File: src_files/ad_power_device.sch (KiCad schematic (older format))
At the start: 19 parts, among them J1 SPEAKER, J2 5622-6309-ML, J5 3-1734592-0, J6 3-1734592-0, Q1 DTC143ZEBTL, Q2 DTC143ZEBTL, U7 QUECTEL_L70-RL

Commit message: all screens added_3 items left
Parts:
- removed J5, J6: 3-1734592-0, greencharge-footprints:TE_3-1734592-0, symbol 3-1734592-0:3-1734592-0
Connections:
- no-connect marks 14 -> 13
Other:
- note added: "DISPLAY_ONE \n GPIOs"
- note added: "TO GPS MODULE"
- note added: "TO HDMI"
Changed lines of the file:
@@
 $Descr A3 16535 11693
 encoding utf-8
-Sheet 1 11
+Sheet 1 12
 Title ""
 Date ""
@@
 F39 "LCD_RST_L_GPIO1_C0_DISPLAY_ONE" I L 7175 3500 39
 F40 "TP_RST_L_GPIO1_C2_DISPLAY_ONE" I L 7175 3575 39
-$EndSheet
-$Sheet
-S 1775 4800 1675 525
-U 61B4DD57
-F0 "OTHER_POWER" 50
-F1 "OTHER_POWER.sch" 50
+F41 "HDMITX_CEC_M0" I L 7175 3700 39
+F42 "HDMITX_SDA" I L 7175 3775 39
+F43 "HDMITX_SCL" I L 7175 3850 39
 $EndSheet
 Wire Notes Line
@@
 F25 "LCD_RST_L_GPIO0_C2_DISPLAY_ONE" I R 9075 4850 39
 F26 "TP_RST_L_GPIO0_C5_DISPLAY_ONE" I R 9075 4925 39
+F27 "HDMITX_CEC_M0" I L 7150 5875 39
+F28 "HDMITX_SDA" I L 7150 5950 39
+F29 "HDMITX_SCL" I L 7150 6025 39
 $EndSheet
 Wire Wire Line
@@
 $EndComp
 $Comp
-L 3-1734592-0:3-1734592-0 J5
-U 1 1 63BB8359
-P -2425 10075
-F 0 "J5" V -2050 10025 50  0000 C CNN
-F 1 "3-1734592-0" V -1959 10025 50  0000 C CNN
-F 2 "greencharge-footprints:TE_3-1734592-0" H -2425 10075 50  0001 L BNN
-F 3 "" H -2425 10075 50  0001 L BNN
-F 4 "TE Connectivity" H -2425 10075 50  0001 L BNN "MANUFACTURER"
-F 5 "2.05mm" H -2425 10075 50  0001 L BNN "MAXIMUM_PACKAGE_HEIGHT"
-F 6 "Manufacturer Recommendations" H -2425 10075 50  0001 L BNN "STANDARD"
-F 7 "C" H -2425 10075 50  0001 L BNN "PARTREV"
-	1    -2425 10075
-	0    1    1    0
-$EndComp
-$Comp
-L 3-1734592-0:3-1734592-0 J6
-U 1 1 63BBAD77
-P -2775 11975
-F 0 "J6" V -2400 11925 50  0000 C CNN
-F 1 "3-1734592-0" V -2309 11925 50  0000 C CNN
-F 2 "greencharge-footprints:TE_3-1734592-0" H -2775 11975 50  0001 L BNN
-F 3 "" H -2775 11975 50  0001 L BNN
-F 4 "TE Connectivity" H -2775 11975 50  0001 L BNN "MANUFACTURER"
-F 5 "2.05mm" H -2775 11975 50  0001 L BNN "MAXIMUM_PACKAGE_HEIGHT"
-F 6 "Manufacturer Recommendations" H -2775 11975 50  0001 L BNN "STANDARD"
-F 7 "C" H -2775 11975 50  0001 L BNN "PARTREV"
-	1    -2775 11975
-	0    1    1    0
-$EndComp
-$Comp
 L Mechanical:MountingHole H1
 U 1 1 63BD71C6
@@
 	11700 6250 11700 9850
 NoConn ~ 12275 7825
-NoConn ~ -1650 10275
 Text Label 7025 7625 2    39   ~ 0
 I2C2_SDA_M0_TP
@@
 Wire Wire Line
 	9075 4925 9225 4925
+Text Label 7025 3700 2    39   ~ 0
+HDMITX_CEC_M0
+Text Label 7025 3775 2    39   ~ 0
+HDMITX_SDA
+Text Label 7025 3850 2    39   ~ 0
+HDMITX_SCL
+Wire Wire Line
+	7175 3700 7025 3700
+Wire Wire Line
+	7175 3775 7025 3775
+Wire Wire Line
+	7175 3850 7025 3850
+Text Label 6750 5875 2    39   ~ 0
+HDMITX_CEC_M0
+Text Label 6750 5950 2    39   ~ 0
+HDMITX_SDA
+Text Label 6750 6025 2    39   ~ 0
+HDMITX_SCL
+Wire Wire Line
+	7150 5875 6750 5875
+Wire Wire Line
+	6750 5950 7150 5950
+Wire Wire Line
+	6750 6025 7150 6025
+Wire Notes Line
+	6650 5775 6250 5775
+Wire Notes Line
+	6250 5775 6250 6075
+Wire Notes Line
+	6250 6075 6750 6075
+Text Notes 6250 5800 3    39   ~ 0
+TO HDMI
+$Sheet
+S 1775 4800 1675 525
+U 61B4DD57
+F0 "OTHER_POWER" 50
+F1 "OTHER_POWER.sch" 50
+$EndSheet
+Text Notes 10050 4400 2    39   ~ 0
+TO GPS MODULE
+Wire Notes Line
+	9550 4475 9375 4475
+Wire Notes Line
+	9550 4300 9550 4475
+Wire Notes Line
+	9400 4300 9550 4300
+Wire Notes Line
+	9900 4475 10275 4475
+Wire Notes Line
+	10275 4475 10275 4950
+Wire Notes Line
+	10275 4950 10050 4950
+Text Notes 10400 4925 1    39   ~ 0
+DISPLAY_ONE \n   GPIOs
 $EndSCHEMATC

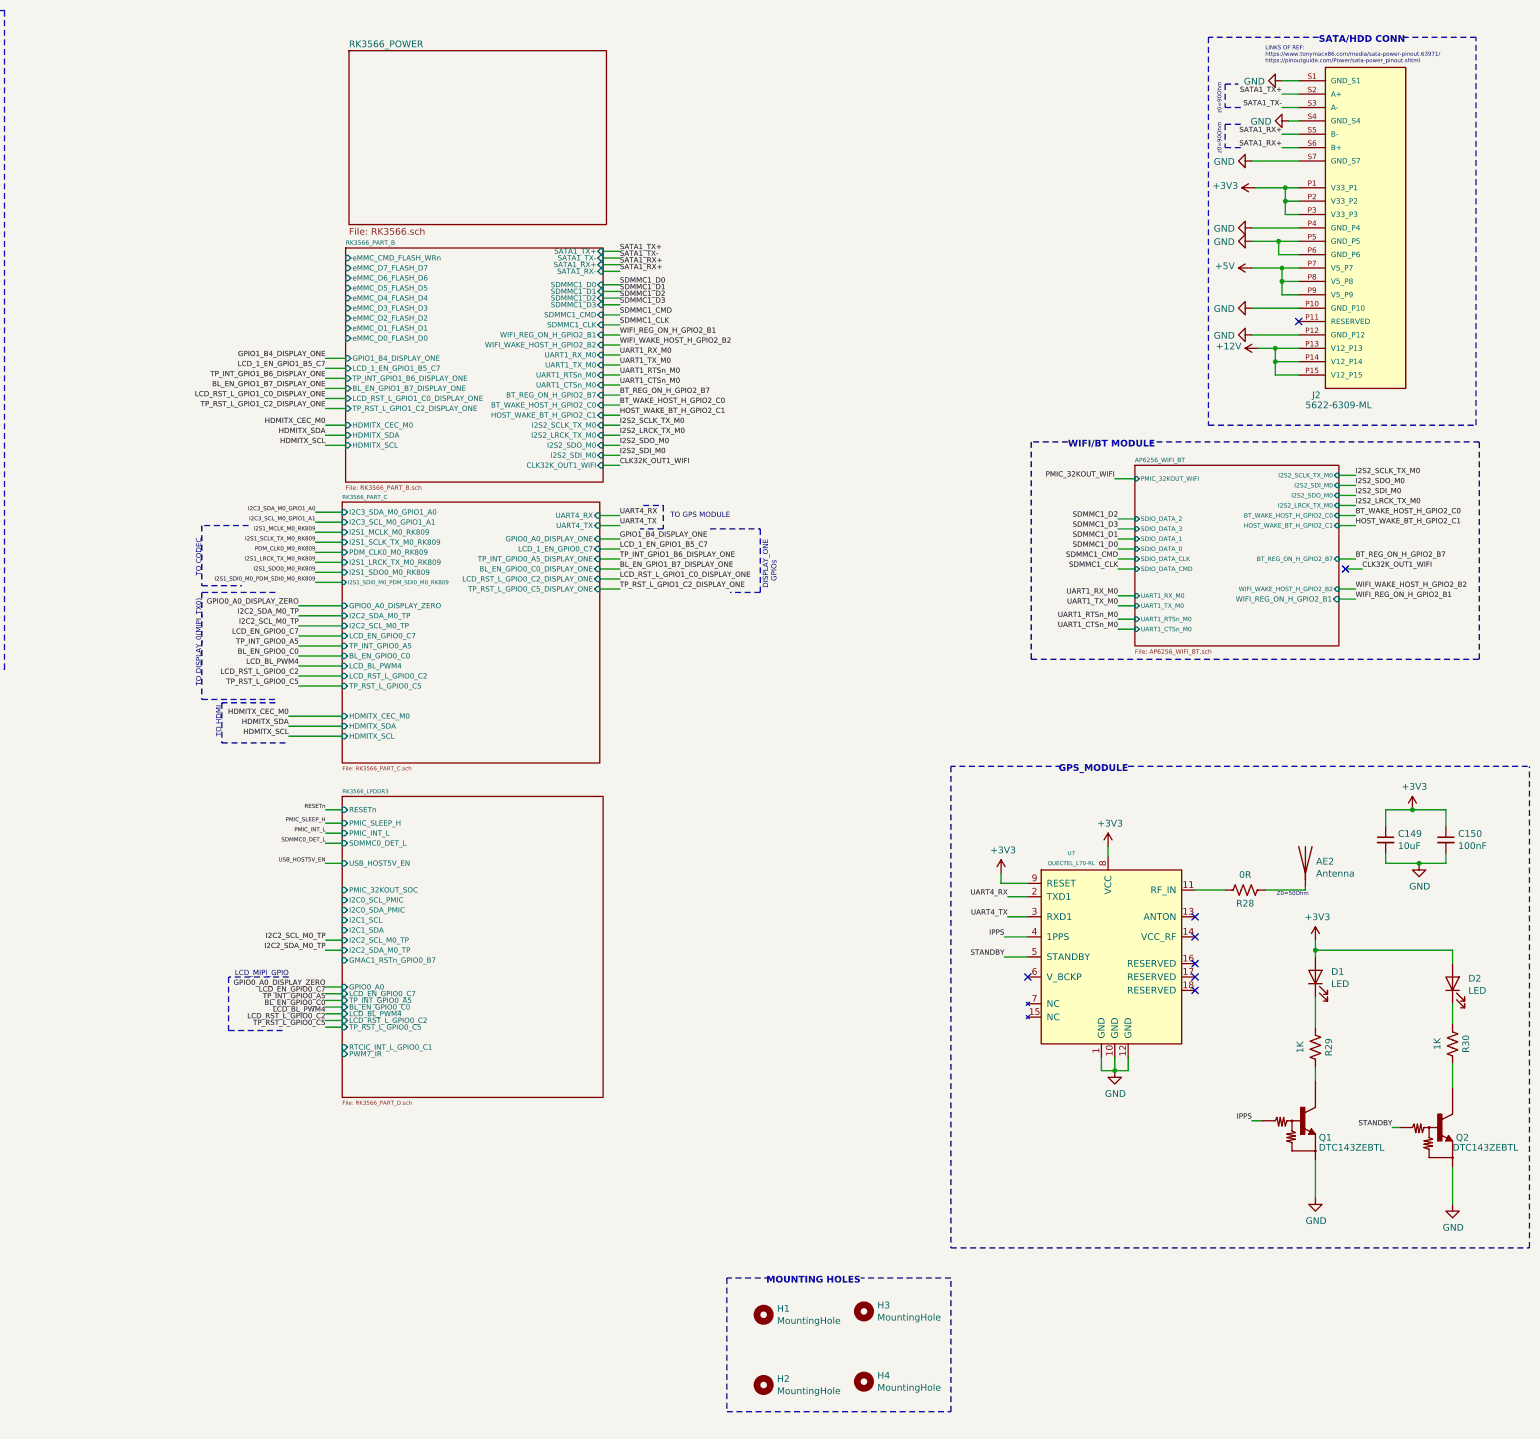
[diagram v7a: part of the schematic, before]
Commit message: updated 4G module and simcard
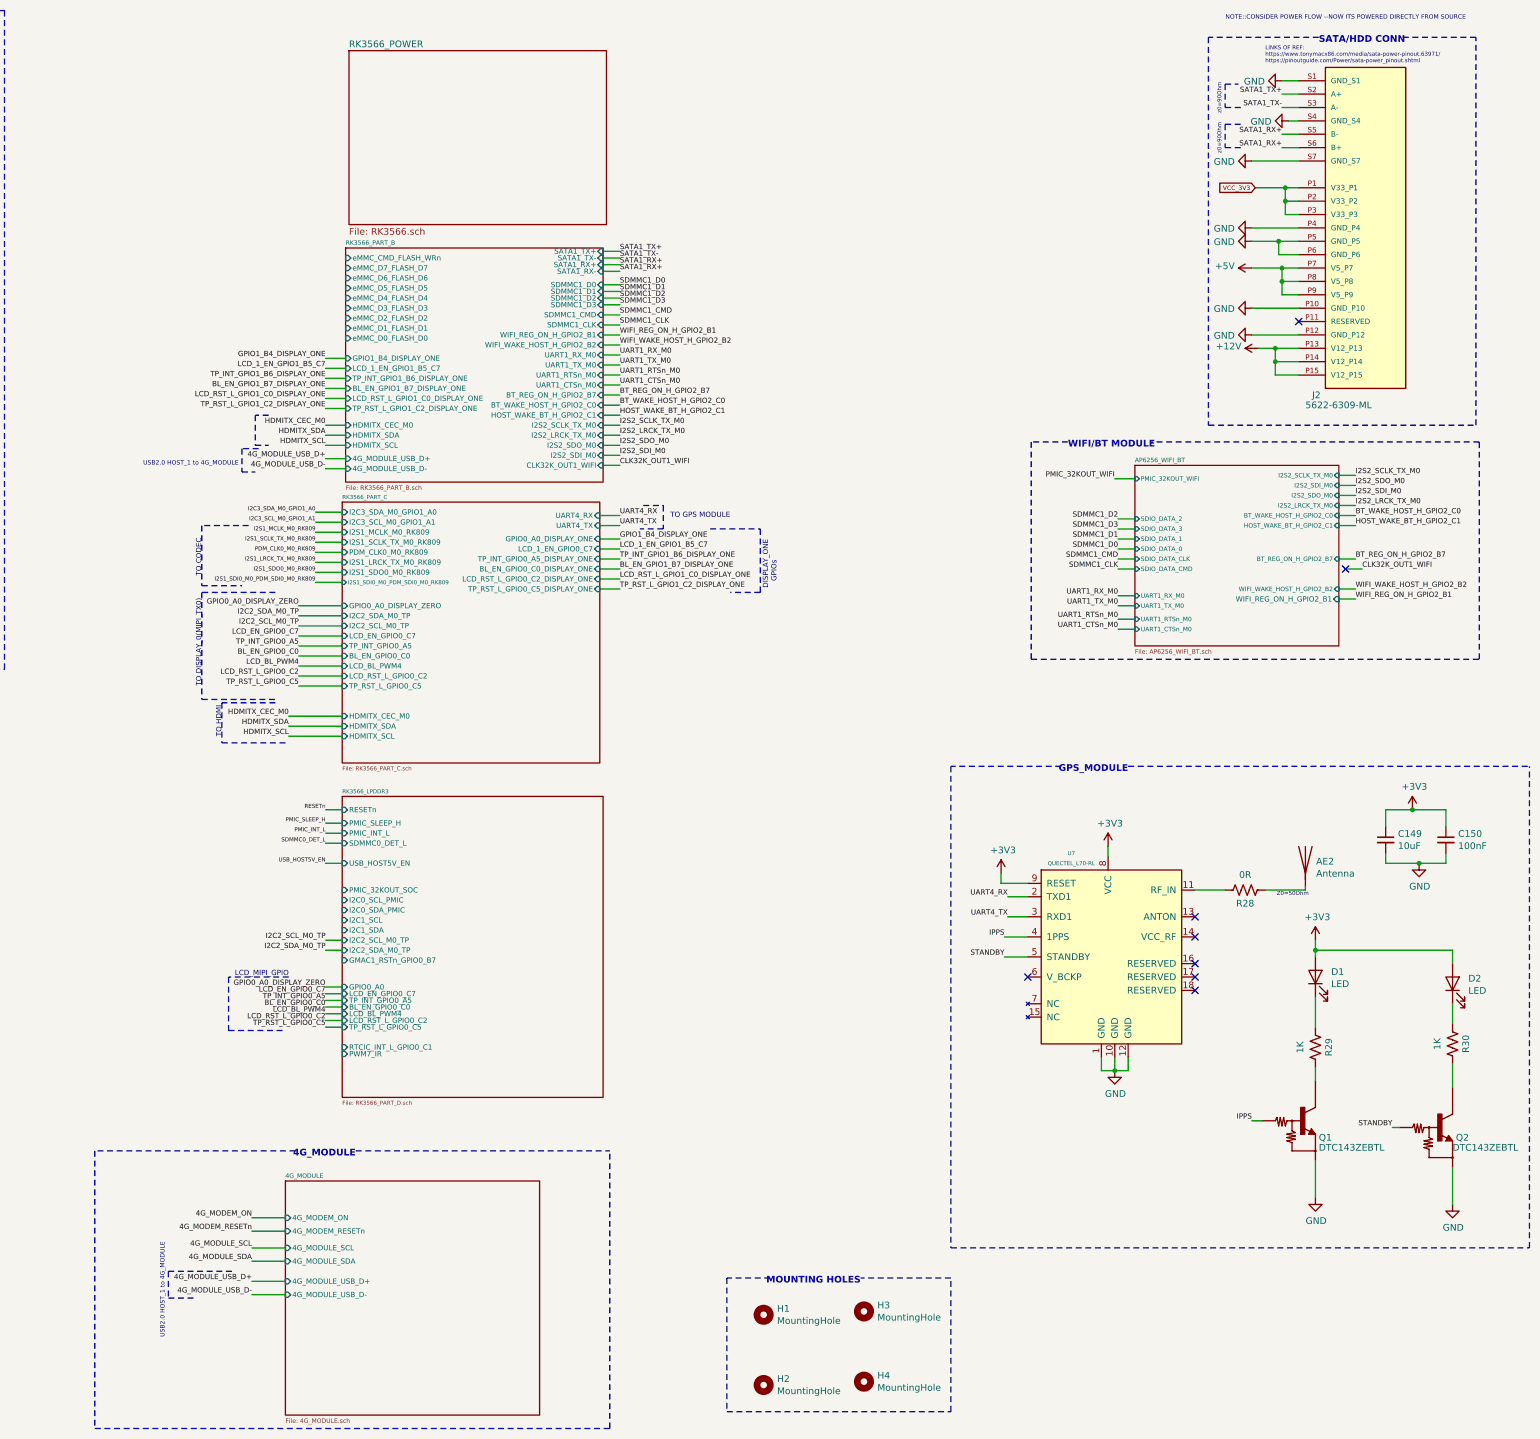
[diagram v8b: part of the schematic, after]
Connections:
- net +3V3: no longer J2.P1 (V33_P1), J2.P2 (V33_P2), J2.P3 (V33_P3)
- new net VCC_3V3: J2.P1 (V33_P1), J2.P2 (V33_P2), J2.P3 (V33_P3)
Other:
- note added: "4G_MODULE\n"
- note added: "NOTE::CONSIDER POWER FLOW --NOW ITS POWERED DIRECTLY FROM SOURCE"
- note added: "USB2.0 HOST_1 to 4G_MODULE"
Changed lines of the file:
@@
 $Descr A3 16535 11693
 encoding utf-8
-Sheet 1 12
+Sheet 1 13
 Title ""
 Date ""
@@
 F42 "HDMITX_SDA" I L 7175 3775 39
 F43 "HDMITX_SCL" I L 7175 3850 39
+F44 "4G_MODULE_USB_D+" I L 7175 3950 39
+F45 "4G_MODULE_USB_D-" I L 7175 4025 39
 $EndSheet
 Wire Notes Line
@@
 Text Notes 14050 1000 0    30   ~ 0
 LINKS OF REF:\nhttps://www.tonymacx86.com/media/sata-power-pinout.63971/\nhttps://pinoutguide.com/Power/sata-power_pinout.shtml
-$Comp
-L power:+3V3 #PWR0107
-U 1 1 61C029C4
-P 13975 1925
-F 0 "#PWR0107" H 13975 1775 50  0001 C CNN
-F 1 "+3V3" V 13990 2053 50  0000 L CNN
-F 2 "" H 13975 1925 50  0001 C CNN
-F 3 "" H 13975 1925 50  0001 C CNN
-	1    13975 1925
-	0    -1   -1   0
-$EndComp
 Wire Wire Line
 	14300 1925 14200 1925
@@
 $EndComp
 Wire Notes Line
-	11700 9850 16025 9850
-Wire Notes Line
 	16025 9850 16025 6250
 Wire Notes Line
@@
 Text Notes 10400 4925 1    39   ~ 0
 DISPLAY_ONE \n   GPIOs
+$Sheet
+S 6725 9350 1900 1750
+U 64C7F7B0
+F0 "4G_MODULE" 33
+F1 "4G_MODULE.sch" 33
+F2 "4G_MODEM_ON" I L 6725 9625 39
+F3 "4G_MODEM_RESETn" I L 6725 9725 39
+F4 "4G_MODULE_SCL" I L 6725 9850 39
+F5 "4G_MODULE_SDA" I L 6725 9950 39
+F6 "4G_MODULE_USB_D+" I L 6725 10100 39
+F7 "4G_MODULE_USB_D-" I L 6725 10200 39
+$EndSheet
+Text GLabel 13975 1925 0    33   Input ~ 0
+VCC_3V3
+Text Notes 15550 675  2    33   ~ 0
+NOTE::CONSIDER POWER FLOW --NOW ITS POWERED DIRECTLY FROM SOURCE
+Wire Notes Line
+	11700 9850 16025 9850
+Text Label 6475 10100 2    39   ~ 0
+4G_MODULE_USB_D+
+Text Label 6475 10200 2    39   ~ 0
+4G_MODULE_USB_D-
+Wire Wire Line
+	6725 10100 6475 10100
+Wire Wire Line
+	6725 10200 6475 10200
+Text Label 6475 9850 2    39   ~ 0
+4G_MODULE_SCL
+Text Label 6475 9950 2    39   ~ 0
+4G_MODULE_SDA
+Text Label 6475 9625 2    39   ~ 0
+4G_MODEM_ON
+Text Label 6475 9725 2    39   ~ 0
+4G_MODEM_RESETn
+Wire Wire Line
+	6725 9850 6475 9850
+Wire Wire Line
+	6725 9950 6475 9950
+Wire Wire Line
+	6725 9625 6475 9625
+Wire Wire Line
+	6725 9725 6475 9725
+Text Notes 5825 10525 1    33   ~ 0
+USB2.0 HOST_1 to 4G_MODULE
+Wire Notes Line
+	6325 10025 5850 10025
+Wire Notes Line
+	5850 10025 5850 10225
+Wire Notes Line
+	5850 10225 6050 10225
+Text Notes 7250 9175 2    50   ~ 10
+4G_MODULE\n
+Wire Notes Line
+	6800 9125 5300 9125
+Wire Notes Line
+	5300 9125 5300 11200
+Wire Notes Line
+	5300 11200 9150 11200
+Wire Notes Line
+	9150 11200 9150 9125
+Wire Notes Line
+	7250 9125 9150 9125
+Text Label 7025 3950 2    39   ~ 0
+4G_MODULE_USB_D+
+Text Label 7025 4025 2    39   ~ 0
+4G_MODULE_USB_D-
+Wire Wire Line
+	7175 3950 7025 3950
+Wire Wire Line
+	7175 4025 7025 4025
+Text Notes 6375 4008 2    33   ~ 0
+USB2.0 HOST_1 to 4G_MODULE
+Wire Notes Line
+	6525 3875 6400 3875
+Wire Notes Line
+	6400 3875 6400 4050
+Wire Notes Line
+	6400 4050 6500 4050
+Wire Notes Line
+	6600 3625 6500 3625
+Wire Notes Line
+	6500 3625 6500 3850
+Wire Notes Line
+	6500 3850 6600 3850
 $EndSCHEMATC
